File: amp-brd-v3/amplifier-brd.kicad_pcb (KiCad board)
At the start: 4 copper layers, 32.5 x 30 mm, 30 parts, among them J1 VOUT, J2 VOUT, Q1 BSS84, U2 INA233, U3 DS28EA00, U4 LMR36510ADDA

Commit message: Modified DAC, AMP v2 and Mezzanine to support AMP v3. Finished AMP v3 design.
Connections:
- BOT1 pad 38: GND -> /EN
- TOP1 pad 38: GND -> /EN
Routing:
- net /EN: track 0.00 -> 34.3 mm, vias 0 -> 1
- net /CTRL_A: track 13.5 -> 25.7 mm, vias 0 -> 1
- net /OP AMP/V_{RAW}: track 0.00 -> 8.62 mm
- net /OP AMP/V_{OUT}: track 0.00 -> 3.28 mm
- net /ONEWIRE: track 21.3 -> 20.0 mm
- net +3V3: track 54.7 -> 55.2 mm, vias 1 -> 2
- net GND: vias 41 -> 118
- added copper zone on F.Cu, net /OP AMP/V_{OUT}
- added copper zone on F.Cu, net /OP AMP/V_{RAW}
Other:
- board text removed: "STAT_EN"

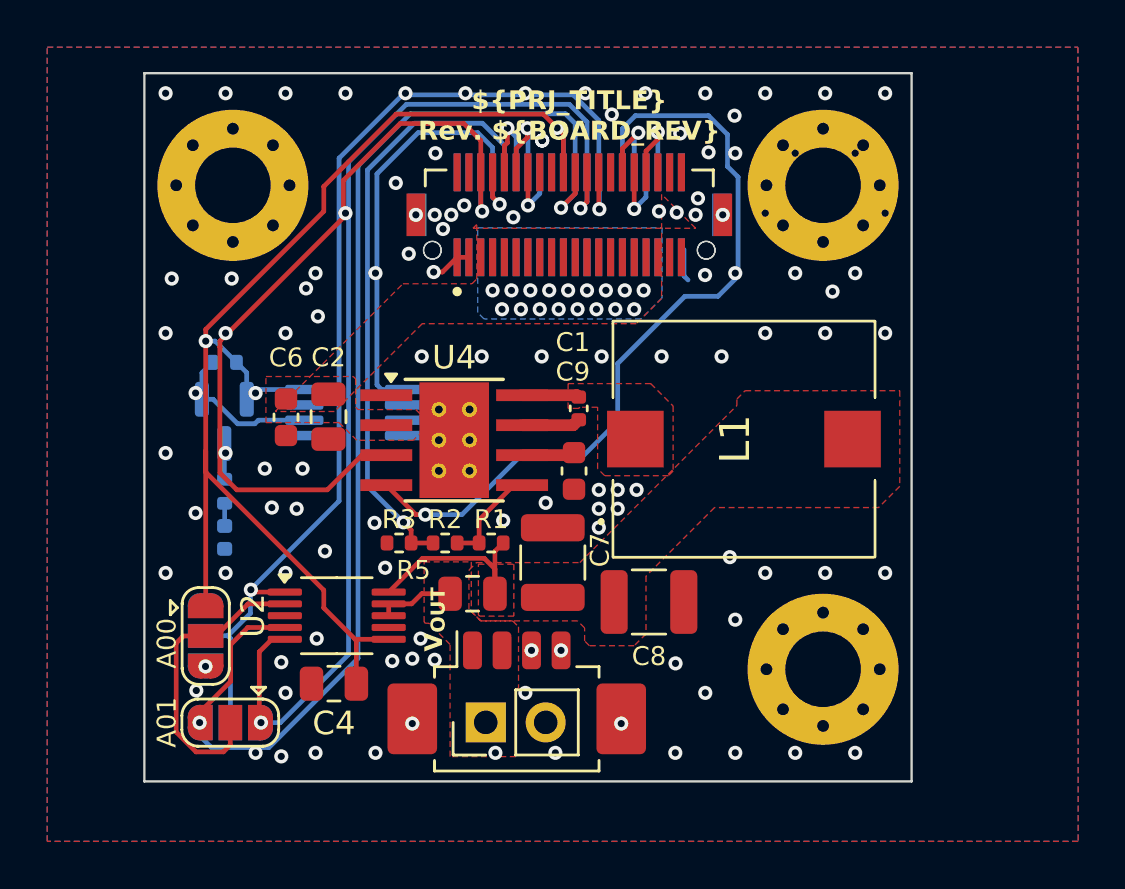
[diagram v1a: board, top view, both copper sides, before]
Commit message: Amp board v3 DRC
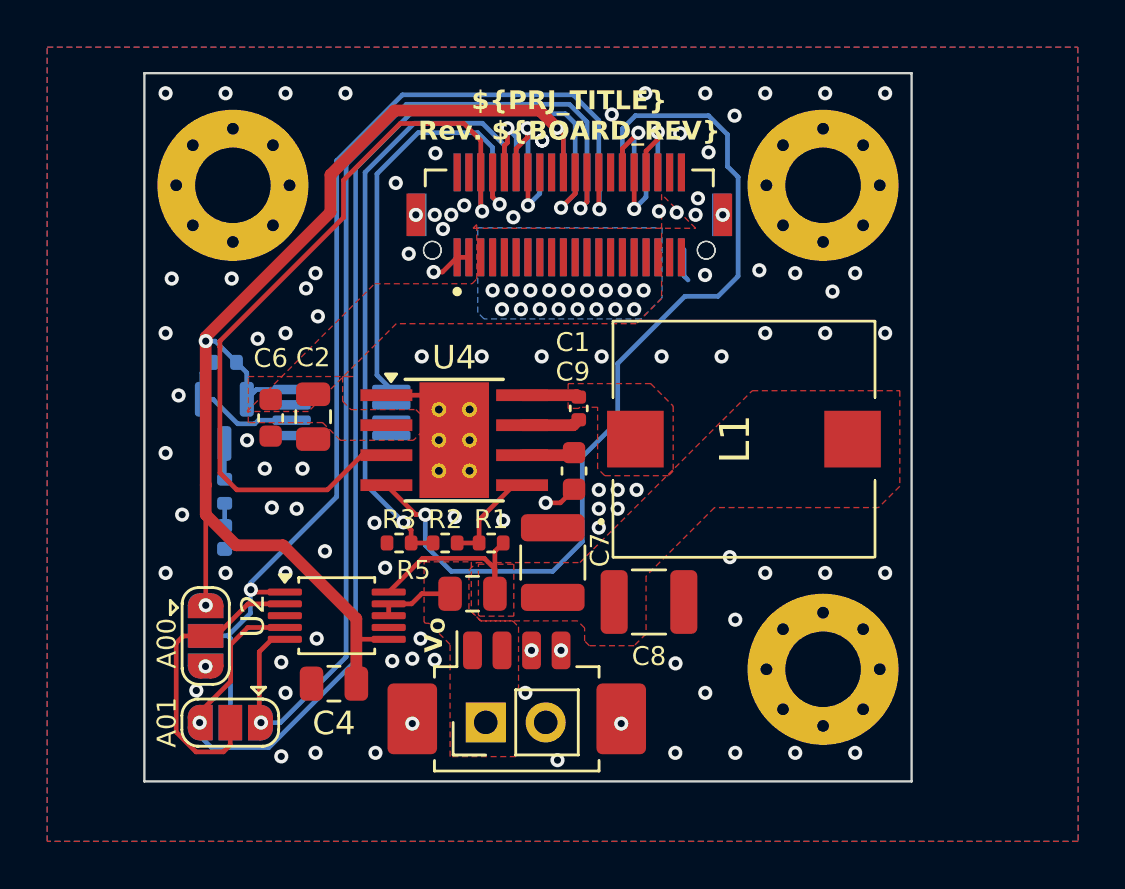
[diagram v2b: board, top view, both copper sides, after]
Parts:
- moved C6 0.65 mm to (218.2, 98.7)
- moved C2 0.65 mm to (220.0, 98.6)
- moved U3 0.54 mm to (221.2, 98.4)
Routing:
- net /STAT_A: track 34.1 -> 38.9 mm
- net GND: track 3.13 -> 7.04 mm, vias 118 -> 104
- net /ONEWIRE: track 20.0 -> 19.3 mm
- net +3V3: track 55.2 -> 55.8 mm, vias 2 -> 3
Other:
- board text added: "V_{O}"
- board text removed: "V_{OUT}"

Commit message: Optimized temperature sensor from Kuravi's design, reworked inductor placement in amp board v3
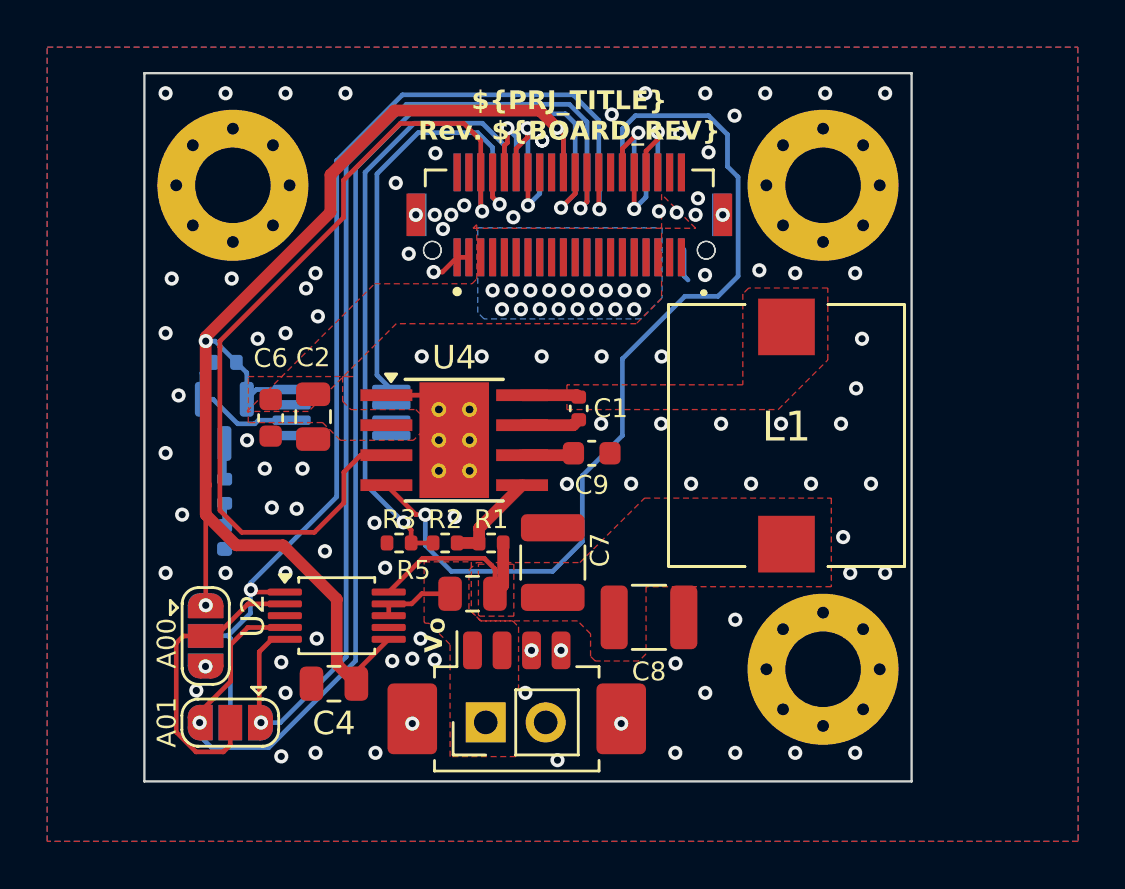
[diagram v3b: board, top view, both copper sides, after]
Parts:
- R7: value 10k -> 100k
- moved L1 1.81 mm to (240.1, 99.4), turned to 0 degrees
- moved C9 1.06 mm to (231.8, 100.2), turned to 0 degrees
- moved C8 0.65 mm to (234.3, 107.1)
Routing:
- net /EN: track 34.3 -> 37.5 mm
- net GND: track 7.04 -> 5.60 mm, vias 104 -> 103
- net +3V3: track 55.8 -> 55.0 mm

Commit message: Final review with Joe
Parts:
- added D2: D_Schottky, Diode_SMD:D_0402_1005Metric, B.Cu at (224.0, 104.6)
- added D3: D_Schottky, Diode_SMD:D_0402_1005Metric, B.Cu at (222.9, 101.7)
- added R4: 0, Resistor_SMD:R_0402_1005Metric, B.Cu at (222.9, 100.7)
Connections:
- R2 pad 2: /CTRL_A -> /OP AMP/FCTRL
- R3 pad 2: /CTRL_A -> /OP AMP/FCTRL
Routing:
- net /OP AMP/FCTRL: track 0.00 -> 5.61 mm, vias 0 -> 1
- net /CTRL_A: track 25.7 -> 22.1 mm, vias 1 -> 0

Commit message: Tested DAC and INA, doing new boards
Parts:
- added R8: 10k, Resistor_SMD:R_0402_1005Metric, B.Cu at (221.2, 111.5)
- added R9: 10k, Resistor_SMD:R_0402_1005Metric, B.Cu at (219.7, 109.6)
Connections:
- U3 pad 7: unconnected-(U3-PIOB-Pad7) -> GND
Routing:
- net +3V3: track 55.0 -> 57.7 mm, vias 3 -> 5
- net /SDA: track 52.2 -> 53.0 mm

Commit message: Updated all boards for production
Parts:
- removed J2: VOUT, Connector_PinHeader_2.54mm:PinHeader_1x02_P2.54mm_Vertical
- J1: footprint Connector_Molex:Molex_PicoBlade_53261-0471_1x04-1MP_P1.25mm_Horizontal -> Connector_Molex:Molex_PicoBlade_53261-0271_1x02-1MP_P1.25mm_Horizontal
- R3: value 10k -> 100k
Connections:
- J1 pad 2: /OP AMP/V_{OUT} -> GND
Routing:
- net GND: track 5.60 -> 15.0 mm

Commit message: Added part numbers
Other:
- board text added: "Designer: ${DESIGNER} Reviewer: ${REVIEWER} ${COMPANY}"
- board text removed: "Designer: ${DESIGNER} Reviewer: ${REVIEWER}"
